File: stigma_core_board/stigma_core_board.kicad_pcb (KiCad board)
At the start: 4 copper layers, 40 x 40 mm, 84 parts, among them J1 TC2050, J5 USB_C_Receptacle_USB2.0, SW1 KMR721NGLFS, SW2 KMR721NGLFS, U1 STM32H743VITx, U10 H3LIS331DL, U11 MS5607/MS5611, U12 LIS3MDL, U13 BMP580/BMP388/LPS22, U2 TPD4E1U06, U3 BMP580/BMP388/LPS22, U4 IIM-42652 (or other LGA-14 IM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, U5 AZ1117I-3.3, U6 ICM-42688 (or other LGA-14 IM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, U8 W25Q128JVP, U9 LSM6DSR, Y1 25MHz, Y2 32.768kHz

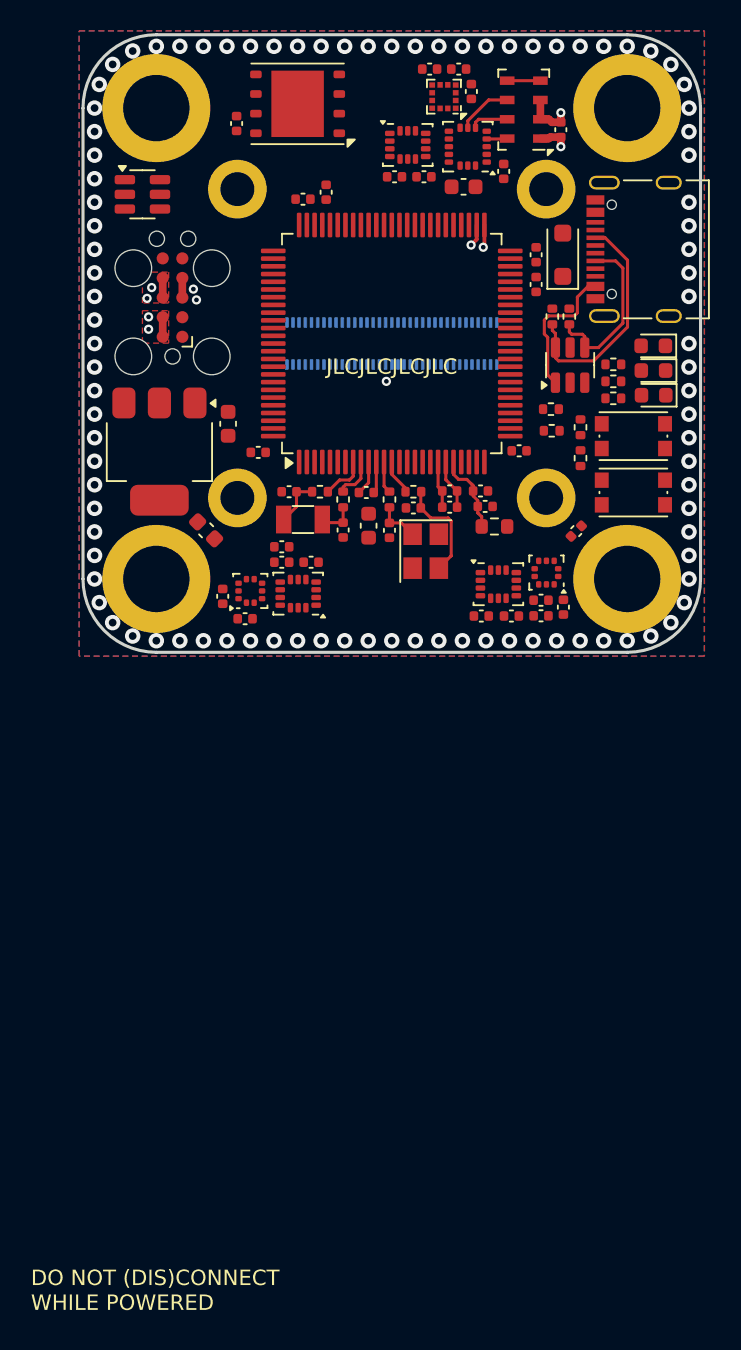
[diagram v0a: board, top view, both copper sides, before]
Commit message: Restore stigma_core_board from 4524638
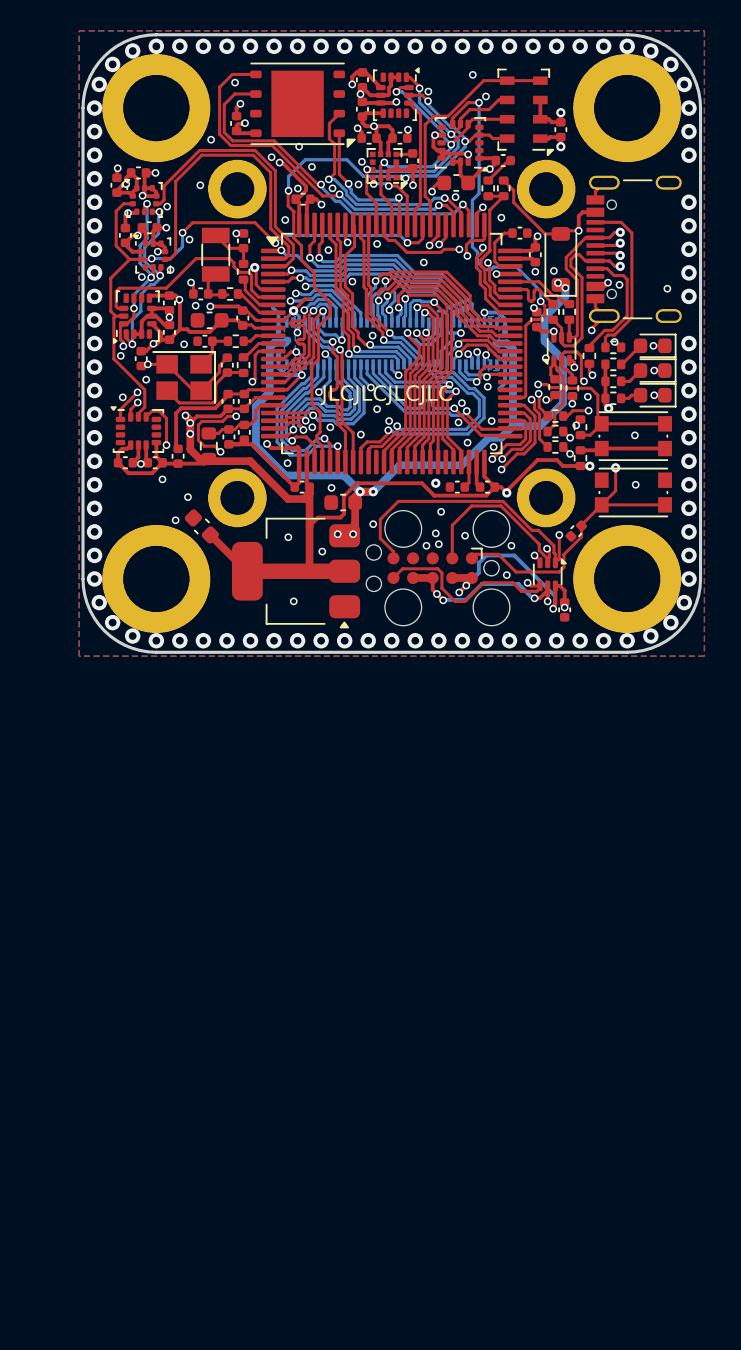
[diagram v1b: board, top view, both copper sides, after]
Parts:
- removed REF**: DF40GB-70DP-0.4V, stigma:DF40GB-70DP-0.4V
- removed the U2 at (99.1, 105.6)
- added C39: 100n, Capacitor_SMD:C_0402_1005Metric, F.Cu at (126.5, 132.5)
- added C40: 100n, Capacitor_SMD:C_0402_1005Metric, F.Cu at (124.7, 113.7)
- added J3: ~, stigma:DF40GB-70DP-0.4V-plug, B.Cu at (115.2, 115.2)
- added R14: 4k7, Resistor_SMD:R_0402_1005Metric, F.Cu at (122.5, 105.2)
- added R15: 10k, Resistor_SMD:R_0402_1005Metric, F.Cu at (121.5, 105.2)
- added R16: 22, Resistor_SMD:R_0402_1005Metric, F.Cu at (125.8, 121.0)
- added R17: 22, Resistor_SMD:R_0402_1005Metric, F.Cu at (127.0, 118.2)
- added R18: 22, Resistor_SMD:R_0402_1005Metric, F.Cu at (125.8, 120.0)
- added R19: 22, Resistor_SMD:R_0402_1005Metric, F.Cu at (125.8, 122.0)
- added R20: 22, Resistor_SMD:R_0402_1005Metric, F.Cu at (125.8, 118.1)
- added U7: TPD4E1U06, Package_TO_SOT_SMD:SOT-563, F.Cu at (125.4, 130.2)
- D1: value LED_Small -> red
- D2: value LED_Small -> yellow
- D3: value LED_Small -> green
- D4: footprint Diode_SMD:D_SOD-123F -> Diode_SMD:D_SOD-123
- R7, R8, R9: value 680 -> 1k
- U13: value BMP580/BMP388/LPS22 -> BMP580
- U2: footprint Package_TO_SOT_SMD:SOT-23-6 -> Package_TO_SOT_SMD:SOT-563
- U3: value BMP580/BMP388/LPS22 -> LPS22
- U4: value IIM-42652 (or other LGA-14 IMU) -> ICM-42670-P
- U6: value ICM-42688 (or other LGA-14 IMU) -> ICM-42688-P
- moved C30 39.3 mm to (98.8, 104.2), turned to 180 degrees
- moved C29 38.4 mm to (97.5, 105.0), turned to -90 degrees
- moved U3 35.5 mm to (99.2, 106.0), turned to 0 degrees
- moved C35 26.0 mm to (98.0, 108.2), turned to -90 degrees
- moved C37 25.7 mm to (101.4, 122.5), turned to -90 degrees
- moved U6 25.3 mm to (98.8, 120.9)
- moved C31 25.1 mm to (99.9, 123.0)
- moved C32 25.1 mm to (98.0, 123.0)
- moved C36 24.3 mm to (99.5, 107.8), turned to 180 degrees
- moved J1 24.3 mm to (117.9, 129.8), turned to 180 degrees
- moved U13 22.6 mm to (99.8, 109.5), turned to 0 degrees
- moved U4 20.8 mm to (98.8, 113.5), turned to 90 degrees
- moved Y1 19.3 mm to (101.8, 117.5), turned to 180 degrees
- moved FB1 19.2 mm to (103.4, 121.9), turned to 90 degrees
- moved C34 18.3 mm to (100.9, 112.6), turned to 90 degrees
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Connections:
- net Net-(C10-Pad1) renamed /VCAP2
- net Net-(C9-Pad1) renamed /VCAP1
- C19 pad 2: +3V3 -> +3.3V
- C21 pad 2: +3V3 -> +3.3V
- C22 pad 2: +3V3 -> +3.3V
- C23 pad 2: +3V3 -> +3.3V
- C24 pad 2: +3V3 -> +3.3V
- C25 pad 2: +3V3 -> +3.3V
- C26 pad 2: +3V3 -> +3.3V
- C27 pad 2: +3V3 -> +3.3V
- C29 pad 2: +3V3 -> +3.3V
- C30 pad 2: +3V3 -> +3.3V
- C31 pad 2: +3V3 -> +3.3V
- C32 pad 2: +3V3 -> +3.3V
- C33 pad 2: +3V3 -> +3.3V
- C34 pad 2: +3V3 -> +3.3V
- C35 pad 2: +3V3 -> +3.3V
- C36 pad 2: +3V3 -> +3.3V
- C37 pad 2: +3V3 -> +3.3V
- C38 pad 2: +3V3 -> +3.3V
- D4 pad 2: Net-(D4-A) -> /VBUS
- J1 pad 2: SWDIO -> /J1-SWDIO
- J1 pad 5: SWO -> /J1-SWO
- J1 pad 6: SWCLK -> Net-(J1-Pin_6)
- J5 pad A4: Net-(D4-A) -> /VBUS
- J5 pad A9: Net-(D4-A) -> /VBUS
- J5 pad B4: Net-(D4-A) -> /VBUS
- J5 pad B9: Net-(D4-A) -> /VBUS
- R6 pad 2: +3V3 -> +3.3V
- U1 pad 1: SPI4_SCK -> PE2
- U1 pad 14: NRST -> Net-(U1-NRST)
- U1 pad 15: unconnected-(U1-PC0-Pad15) -> PC0
- U1 pad 16: ETH_MDC -> PC1_ETH_MDC
- U1 pad 17: SPI2_MISO -> PC2_C
- U1 pad 18: SPI2_MOSI -> PC3_C
- U1 pad 2: unconnected-(U1-PE3-Pad2) -> SPI2_CS_BARO3
- U1 pad 22: unconnected-(U1-PA0-Pad22) -> PA0
- U1 pad 23: ETH_REF_CLK -> PA1_ETH_REF_CLK
- U1 pad 24: ETH_MDIO -> PA2_ETH_MDIO
- U1 pad 25: unconnected-(U1-PA3-Pad25) -> PA3
- U1 pad 28: unconnected-(U1-PA4-Pad28) -> PA4
- U1 pad 3: unconnected-(U1-PE4-Pad3) -> SPI2_CS_BARO2
- U1 pad 30: SPI1_MISO -> PA6
- U1 pad 31: ETH_CRS_DV -> PA7_ETH_CRS_DV
- U1 pad 32: ETH_RXD0 -> ETH_RXD-
- U1 pad 33: ETH_RXD1 -> ETH_RXD+
- U1 pad 34: unconnected-(U1-PB0-Pad34) -> PB0
- U1 pad 35: unconnected-(U1-PB1-Pad35) -> PB1
- U1 pad 37: unconnected-(U1-PE7-Pad37) -> PE7
- U1 pad 38: unconnected-(U1-PE8-Pad38) -> PE8
- U1 pad 39: unconnected-(U1-PE9-Pad39) -> PE9
- U1 pad 4: SPI4_MISO -> PE5
- U1 pad 40: unconnected-(U1-PE10-Pad40) -> PE10
- U1 pad 41: unconnected-(U1-PE11-Pad41) -> PE11
- U1 pad 42: unconnected-(U1-PE12-Pad42) -> PE12
- U1 pad 43: unconnected-(U1-PE13-Pad43) -> PE13
- U1 pad 44: unconnected-(U1-PE14-Pad44) -> PE14
- U1 pad 46: unconnected-(U1-PB10-Pad46) -> PB10
- U1 pad 47: ETH_TX_EN -> PB11_ETH_TX_EN
- U1 pad 5: SPI4_MOSI -> PE6
- U1 pad 51: ETH_TXD0 -> ETH_TXD-
- U1 pad 52: ETH_TXD1 -> ETH_TXD+
- U1 pad 53: USB_D- -> SPI2_MISO
- U1 pad 54: USB_D+ -> SPI2_MOSI
- U1 pad 55: unconnected-(U1-PD8-Pad55) -> SPI2_CS_IMU2
- U1 pad 56: unconnected-(U1-PD9-Pad56) -> SPI1_CS_HIGHG
- U1 pad 59: unconnected-(U1-PD12-Pad59) -> PD12
- U1 pad 60: unconnected-(U1-PD13-Pad60) -> PD13
- U1 pad 61: unconnected-(U1-PD14-Pad61) -> PD14
- U1 pad 62: unconnected-(U1-PD15-Pad62) -> PD15
- U1 pad 63: unconnected-(U1-PC6-Pad63) -> PC6
- U1 pad 64: unconnected-(U1-PC7-Pad64) -> PC7
- U1 pad 65: unconnected-(U1-PC8-Pad65) -> PC8
- U1 pad 66: unconnected-(U1-PC9-Pad66) -> PC9
- U1 pad 67: unconnected-(U1-PA8-Pad67) -> LED_RED
- U1 pad 69: unconnected-(U1-PA10-Pad69) -> LED_YELLOW
- U1 pad 7: unconnected-(U1-PC13-Pad7) -> SPI2_CS_IMU3
- U1 pad 70: CAN1_RX -> USB_D-
- U1 pad 71: CAN1_TX -> USB_D+
- U1 pad 77: unconnected-(U1-PA15-Pad77) -> LED_GREEN
- U1 pad 81: unconnected-(U1-PD0-Pad81) -> PD0
- U1 pad 82: unconnected-(U1-PD1-Pad82) -> PD1
- U1 pad 83: unconnected-(U1-PD2-Pad83) -> SPI1_CS_BARO1
- U1 pad 85: unconnected-(U1-PD4-Pad85) -> SPI1_CS_IMU1
- U1 pad 86: unconnected-(U1-PD5-Pad86) -> SPI1_CS_MAG
- U1 pad 87: unconnected-(U1-PD6-Pad87) -> SPI3_CS_FLASH
- U1 pad 90: unconnected-(U1-PB4-Pad90) -> SPI1_MISO
- U1 pad 91: CAN2_RX -> PB5
- U1 pad 92: CAN2_TX -> PB6
- U1 pad 93: unconnected-(U1-PB7-Pad93) -> PB7
- U1 pad 94: BOOT0 -> Net-(U1-BOOT0)
- U1 pad 95: unconnected-(U1-PB8-Pad95) -> PB8
- U1 pad 96: unconnected-(U1-PB9-Pad96) -> PB9
- U1 pad 97: unconnected-(U1-PE0-Pad97) -> PE0
- U1 pad 98: unconnected-(U1-PE1-Pad98) -> PE1
- U10 pad 1: +3V3 -> +3.3V
- U10 pad 14: +3V3 -> +3.3V
- U10 pad 15: +3V3 -> +3.3V
- U10 pad 4: SPI1_SCL -> SPI1_SCK
- U10 pad 8: SPI1_CS_ACC -> SPI1_CS_HIGHG
- U11 pad 1: +3V3 -> +3.3V
- U11 pad 8: SPI1_SCL -> SPI1_SCK
- U12 pad 1: SPI1_SCL -> SPI1_SCK
- U12 pad 5: +3V3 -> +3.3V
- U12 pad 6: +3V3 -> +3.3V
- U13 pad 1: +3V3 -> +3.3V
- U13 pad 10: +3V3 -> +3.3V
- U13 pad 6: SPI1_CS_BARO3 -> SPI2_CS_BARO3
- U2 pad 1: Net-(D4-A) -> BOOT
- U2 pad 2: GND -> NRST
- U2 pad 3: unconnected-(U2-IO2-Pad3) -> GND
- U2 pad 4: /D0- -> /D0+
- U2 pad 5: unconnected-(U2-VP-Pad5) -> /D0-
- U2 pad 6: /D0+ -> /VBUS
- U3 pad 1: +3V3 -> +3.3V
- U3 pad 10: +3V3 -> +3.3V
- U3 pad 6: SPI1_CS_BARO2 -> SPI2_CS_BARO2
- U4 pad 12: SPI1_CS_IMU3 -> SPI2_CS_IMU3
- U4 pad 5: +3V3 -> +3.3V
- U4 pad 8: +3V3 -> +3.3V
- U5 pad 2: +3V3 -> +3.3V
- U6 pad 12: SPI1_CS_IMU2 -> SPI2_CS_IMU2
- U6 pad 5: +3V3 -> +3.3V
- U6 pad 8: +3V3 -> +3.3V
- U9 pad 13: SPI1_SCL -> SPI1_SCK
- U9 pad 5: +3V3 -> +3.3V
- U9 pad 8: +3V3 -> +3.3V
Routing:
- net +3.3V: track 6.54 -> 231.6 mm, vias 2 -> 22
- net GND: track 9.82 -> 123.4 mm, vias 98 -> 203
- net +5V: track 1.27 -> 85.8 mm, vias 2 -> 10
- net SPI2_MOSI: track 0.00 -> 50.7 mm, vias 0 -> 6
- net SPI2_MISO: track 0.00 -> 50.1 mm, vias 0 -> 5
- net Net-(U1-NRST): track 0.00 -> 44.1 mm, vias 0 -> 4
- net SPI3_MOSI: track 0.00 -> 43.9 mm, vias 0 -> 3
- net SPI1_SCK: track 0.00 -> 42.9 mm, vias 0 -> 4
- net SPI2_SCK: track 0.00 -> 39.6 mm, vias 0 -> 4
- net SPI3_SCK: track 0.00 -> 39.5 mm, vias 0 -> 3
- net SPI2_CS_IMU2: track 0.00 -> 34.9 mm, vias 0 -> 2
- net SPI3_MISO: track 0.00 -> 32.8 mm, vias 0 -> 3
- net NRST: track 0.00 -> 31.8 mm, vias 0 -> 2
- net LED_GREEN: track 0.00 -> 28.1 mm, vias 0 -> 2
- net /J1-SWDIO: track 0.00 -> 27.7 mm, vias 0 -> 2
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- added copper zone on B.Cu, net +5V
- removed copper zone on F.Cu, net +3.3V
- removed copper zone on F.Cu, net +5V
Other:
- board text removed: "DO NOT (DIS)CONNECT WHILE POWERED"
- board text removed: "S/N"
- board text removed: "stigma"

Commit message: uploaded files to share current not working parts
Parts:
- removed C39, C40: 100n, Capacitor_SMD:C_0402_1005Metric
- removed J3: ~, stigma:DF40GB-70DP-0.4V-plug
- removed R14: 4k7, Resistor_SMD:R_0402_1005Metric
- removed R15: 10k, Resistor_SMD:R_0402_1005Metric
- removed R16, R17, R18, R19, R20: 22, Resistor_SMD:R_0402_1005Metric
- removed U7: TPD4E1U06, Package_TO_SOT_SMD:SOT-563
- added REF**: DF40GB-70DP-0.4V, stigma:DF40GB-70DP-0.4V, B.Cu at (117.5, 115.2)
- added U2: TPD4E1U06, Package_TO_SOT_SMD:SOT-23-6, F.Cu at (99.1, 105.6)
- D1: value red -> LED_Small
- D2: value yellow -> LED_Small
- D3: value green -> LED_Small
- D4: footprint Diode_SMD:D_SOD-123 -> Diode_SMD:D_SOD-123F
- R7, R8, R9: value 1k -> 680
- U13: value BMP580 -> BMP580/BMP388/LPS22
- U2: footprint Package_TO_SOT_SMD:SOT-563 -> Package_TO_SOT_SMD:SOT-23-6
- U3: value LPS22 -> BMP580/BMP388/LPS22
- U4: value ICM-42670-P -> IIM-42652 (or other LGA-14 IMU)
- U6: value ICM-42688-P -> ICM-42688 (or other LGA-14 IMU)
- moved C30 39.3 mm to (126.4, 132.3), turned to 90 degrees
- moved C29 38.4 mm to (124.9, 131.9), turned to 0 degrees
- moved U3 35.5 mm to (125.3, 130.1), turned to 180 degrees
- moved C35 26.0 mm to (105.8, 133.1), turned to 180 degrees
- moved C37 25.7 mm to (124.9, 132.9), turned to 180 degrees
- moved U6 25.3 mm to (122.2, 130.8)
- moved C31 25.1 mm to (123.0, 132.9)
- moved C32 25.1 mm to (121.0, 132.9)
- moved C36 24.3 mm to (104.3, 131.6), turned to -90 degrees
- moved J1 24.3 mm to (101.0, 112.3), turned to 90 degrees
- moved U13 22.6 mm to (106.1, 131.3), turned to 90 degrees
- moved U4 20.8 mm to (109.2, 131.4), turned to 180 degrees
- moved Y1 19.3 mm to (117.5, 128.7), turned to -90 degrees
- moved FB1 19.2 mm to (121.9, 127.1), turned to 180 degrees
- moved C34 18.3 mm to (108.1, 129.4), turned to 0 degrees
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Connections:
- net /VCAP1 renamed Net-(C9-Pad1)
- net /VCAP2 renamed Net-(C10-Pad1)
- C19 pad 2: +3.3V -> +3V3
- C21 pad 2: +3.3V -> +3V3
- C22 pad 2: +3.3V -> +3V3
- C23 pad 2: +3.3V -> +3V3
- C24 pad 2: +3.3V -> +3V3
- C25 pad 2: +3.3V -> +3V3
- C26 pad 2: +3.3V -> +3V3
- C27 pad 2: +3.3V -> +3V3
- C29 pad 2: +3.3V -> +3V3
- C30 pad 2: +3.3V -> +3V3
- C31 pad 2: +3.3V -> +3V3
- C32 pad 2: +3.3V -> +3V3
- C33 pad 2: +3.3V -> +3V3
- C34 pad 2: +3.3V -> +3V3
- C35 pad 2: +3.3V -> +3V3
- C36 pad 2: +3.3V -> +3V3
- C37 pad 2: +3.3V -> +3V3
- C38 pad 2: +3.3V -> +3V3
- D4 pad 2: /VBUS -> Net-(D4-A)
- J1 pad 2: /J1-SWDIO -> SWDIO
- J1 pad 5: /J1-SWO -> SWO
- J1 pad 6: Net-(J1-Pin_6) -> SWCLK
- J5 pad A4: /VBUS -> Net-(D4-A)
- J5 pad A9: /VBUS -> Net-(D4-A)
- J5 pad B4: /VBUS -> Net-(D4-A)
- J5 pad B9: /VBUS -> Net-(D4-A)
- R6 pad 2: +3.3V -> +3V3
- U1 pad 1: PE2 -> SPI4_SCK
- U1 pad 14: Net-(U1-NRST) -> NRST
- U1 pad 15: PC0 -> unconnected-(U1-PC0-Pad15)
- U1 pad 16: PC1_ETH_MDC -> ETH_MDC
- U1 pad 17: PC2_C -> SPI2_MISO
- U1 pad 18: PC3_C -> SPI2_MOSI
- U1 pad 2: SPI2_CS_BARO3 -> unconnected-(U1-PE3-Pad2)
- U1 pad 22: PA0 -> unconnected-(U1-PA0-Pad22)
- U1 pad 23: PA1_ETH_REF_CLK -> ETH_REF_CLK
- U1 pad 24: PA2_ETH_MDIO -> ETH_MDIO
- U1 pad 25: PA3 -> unconnected-(U1-PA3-Pad25)
- U1 pad 28: PA4 -> unconnected-(U1-PA4-Pad28)
- U1 pad 3: SPI2_CS_BARO2 -> unconnected-(U1-PE4-Pad3)
- U1 pad 30: PA6 -> SPI1_MISO
- U1 pad 31: PA7_ETH_CRS_DV -> ETH_CRS_DV
- U1 pad 32: ETH_RXD- -> ETH_RXD0
- U1 pad 33: ETH_RXD+ -> ETH_RXD1
- U1 pad 34: PB0 -> unconnected-(U1-PB0-Pad34)
- U1 pad 35: PB1 -> unconnected-(U1-PB1-Pad35)
- U1 pad 37: PE7 -> unconnected-(U1-PE7-Pad37)
- U1 pad 38: PE8 -> unconnected-(U1-PE8-Pad38)
- U1 pad 39: PE9 -> unconnected-(U1-PE9-Pad39)
- U1 pad 4: PE5 -> SPI4_MISO
- U1 pad 40: PE10 -> unconnected-(U1-PE10-Pad40)
- U1 pad 41: PE11 -> unconnected-(U1-PE11-Pad41)
- U1 pad 42: PE12 -> unconnected-(U1-PE12-Pad42)
- U1 pad 43: PE13 -> unconnected-(U1-PE13-Pad43)
- U1 pad 44: PE14 -> unconnected-(U1-PE14-Pad44)
- U1 pad 46: PB10 -> unconnected-(U1-PB10-Pad46)
- U1 pad 47: PB11_ETH_TX_EN -> ETH_TX_EN
- U1 pad 5: PE6 -> SPI4_MOSI
- U1 pad 51: ETH_TXD- -> ETH_TXD0
- U1 pad 52: ETH_TXD+ -> ETH_TXD1
- U1 pad 53: SPI2_MISO -> USB_D-
- U1 pad 54: SPI2_MOSI -> USB_D+
- U1 pad 55: SPI2_CS_IMU2 -> unconnected-(U1-PD8-Pad55)
- U1 pad 56: SPI1_CS_HIGHG -> unconnected-(U1-PD9-Pad56)
- U1 pad 59: PD12 -> unconnected-(U1-PD12-Pad59)
- U1 pad 60: PD13 -> unconnected-(U1-PD13-Pad60)
- U1 pad 61: PD14 -> unconnected-(U1-PD14-Pad61)
- U1 pad 62: PD15 -> unconnected-(U1-PD15-Pad62)
- U1 pad 63: PC6 -> unconnected-(U1-PC6-Pad63)
- U1 pad 64: PC7 -> unconnected-(U1-PC7-Pad64)
- U1 pad 65: PC8 -> unconnected-(U1-PC8-Pad65)
- U1 pad 66: PC9 -> unconnected-(U1-PC9-Pad66)
- U1 pad 67: LED_RED -> unconnected-(U1-PA8-Pad67)
- U1 pad 69: LED_YELLOW -> unconnected-(U1-PA10-Pad69)
- U1 pad 7: SPI2_CS_IMU3 -> unconnected-(U1-PC13-Pad7)
- U1 pad 70: USB_D- -> CAN1_RX
- U1 pad 71: USB_D+ -> CAN1_TX
- U1 pad 77: LED_GREEN -> unconnected-(U1-PA15-Pad77)
- U1 pad 81: PD0 -> unconnected-(U1-PD0-Pad81)
- U1 pad 82: PD1 -> unconnected-(U1-PD1-Pad82)
- U1 pad 83: SPI1_CS_BARO1 -> unconnected-(U1-PD2-Pad83)
- U1 pad 85: SPI1_CS_IMU1 -> unconnected-(U1-PD4-Pad85)
- U1 pad 86: SPI1_CS_MAG -> unconnected-(U1-PD5-Pad86)
- U1 pad 87: SPI3_CS_FLASH -> unconnected-(U1-PD6-Pad87)
- U1 pad 90: SPI1_MISO -> unconnected-(U1-PB4-Pad90)
- U1 pad 91: PB5 -> CAN2_RX
- U1 pad 92: PB6 -> CAN2_TX
- U1 pad 93: PB7 -> unconnected-(U1-PB7-Pad93)
- U1 pad 94: Net-(U1-BOOT0) -> BOOT0
- U1 pad 95: PB8 -> unconnected-(U1-PB8-Pad95)
- U1 pad 96: PB9 -> unconnected-(U1-PB9-Pad96)
- U1 pad 97: PE0 -> unconnected-(U1-PE0-Pad97)
- U1 pad 98: PE1 -> unconnected-(U1-PE1-Pad98)
- U10 pad 1: +3.3V -> +3V3
- U10 pad 14: +3.3V -> +3V3
- U10 pad 15: +3.3V -> +3V3
- U10 pad 4: SPI1_SCK -> SPI1_SCL
- U10 pad 8: SPI1_CS_HIGHG -> SPI1_CS_ACC
- U11 pad 1: +3.3V -> +3V3
- U11 pad 8: SPI1_SCK -> SPI1_SCL
- U12 pad 1: SPI1_SCK -> SPI1_SCL
- U12 pad 5: +3.3V -> +3V3
- U12 pad 6: +3.3V -> +3V3
- U13 pad 1: +3.3V -> +3V3
- U13 pad 10: +3.3V -> +3V3
- U13 pad 6: SPI2_CS_BARO3 -> SPI1_CS_BARO3
- U2 pad 1: BOOT -> Net-(D4-A)
- U2 pad 2: NRST -> GND
- U2 pad 3: GND -> unconnected-(U2-IO2-Pad3)
- U2 pad 4: /D0+ -> /D0-
- U2 pad 5: /D0- -> unconnected-(U2-VP-Pad5)
- U2 pad 6: /VBUS -> /D0+
- U3 pad 1: +3.3V -> +3V3
- U3 pad 10: +3.3V -> +3V3
- U3 pad 6: SPI2_CS_BARO2 -> SPI1_CS_BARO2
- U4 pad 12: SPI2_CS_IMU3 -> SPI1_CS_IMU3
- U4 pad 5: +3.3V -> +3V3
- U4 pad 8: +3.3V -> +3V3
- U5 pad 2: +3.3V -> +3V3
- U6 pad 12: SPI2_CS_IMU2 -> SPI1_CS_IMU2
- U6 pad 5: +3.3V -> +3V3
- U6 pad 8: +3.3V -> +3V3
- U9 pad 13: SPI1_SCK -> SPI1_SCL
- U9 pad 5: +3.3V -> +3V3
- U9 pad 8: +3.3V -> +3V3
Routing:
- net +3.3V: track 231.6 -> 6.54 mm, vias 22 -> 2
- net GND: track 123.4 -> 9.82 mm, vias 203 -> 98
- net +5V: track 85.8 -> 1.27 mm, vias 10 -> 2
- net SPI2_MOSI: track 50.7 -> 0.00 mm, vias 6 -> 0
- net SPI2_MISO: track 50.1 -> 0.00 mm, vias 5 -> 0
- net Net-(U1-NRST): track 44.1 -> 0.00 mm, vias 4 -> 0
- net SPI3_MOSI: track 43.9 -> 0.00 mm, vias 3 -> 0
- net SPI1_SCK: track 42.9 -> 0.00 mm, vias 4 -> 0
- net SPI2_SCK: track 39.6 -> 0.00 mm, vias 4 -> 0
- net SPI3_SCK: track 39.5 -> 0.00 mm, vias 3 -> 0
- net SPI2_CS_IMU2: track 34.9 -> 0.00 mm, vias 2 -> 0
- net SPI3_MISO: track 32.8 -> 0.00 mm, vias 3 -> 0
- net NRST: track 31.8 -> 0.00 mm, vias 2 -> 0
- net LED_GREEN: track 28.1 -> 0.00 mm, vias 2 -> 0
- net /J1-SWDIO: track 27.7 -> 0.00 mm, vias 2 -> 0
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- added copper zone on F.Cu, net +3.3V
- added copper zone on F.Cu, net +5V
- removed copper zone on B.Cu, net +5V
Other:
- board text added: "DO NOT (DIS)CONNECT WHILE POWERED"
- board text added: "S/N"
- board text added: "stigma"
